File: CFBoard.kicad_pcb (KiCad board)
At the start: 2 copper layers, 80 x 60 mm, 21 parts, among them U1 STM32 Blue Pill, U2 Wemos D1 Mini, U3 GY-6500, U4 BMP180_5pin

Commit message: feat: wrap up version 1
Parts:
- moved R4 45.2 mm to (159.6, 113.2), turned to -90 degrees
- moved R3 27.4 mm to (111.1, 117.7)
- moved C5 25.2 mm to (137.9, 131.7)
- moved R5 18.5 mm to (148.4, 93.2), turned to 180 degrees
- moved C4 17.8 mm to (137.9, 97.2)
- moved U3 17.8 mm to (148.4, 108.7)
- moved REG1 17.8 mm to (170.4, 87.7)
- moved C1 17.8 mm to (154.1, 92.0)
- moved C3 17.8 mm to (158.1, 123.7)
- moved CONN1 17.8 mm to (142.6, 82.0)
- moved REF** 17.8 mm to (185.4, 81.0)
- moved REF** 17.8 mm to (110.9, 81.0)
- moved C2 17.8 mm to (184.9, 89.0)
- moved D2 17.8 mm to (158.1, 132.5)
- moved REF** 17.8 mm to (110.9, 135.5)
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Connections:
- C5 pad 1: Net-(U2-3.3V) -> Net-(D2-A)
- C5 pad 2: Net-(D2-A) -> Net-(U2-3.3V)
- R5 pad 1: Net-(U1-PB9) -> Net-(U3-INT)
- U3 pad 8: Net-(U1-PB9) -> Net-(U3-INT)
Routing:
- net Net-(D2-A): track 0.00 -> 196.8 mm
- net Net-(U2-Rx): track 0.00 -> 119.7 mm
- net Net-(U2-Tx): track 0.00 -> 105.8 mm
- net Net-(U2-3.3V): track 0.00 -> 85.8 mm, vias 0 -> 2
- net Net-(U1-PB8): track 0.00 -> 75.6 mm
- net Net-(U1-PB9): track 0.00 -> 70.1 mm
- net Net-(CONN1-Signal_2): track 0.00 -> 69.0 mm
- net Net-(CONN1-Signal_1): track 0.00 -> 64.9 mm
- net Net-(CONN1-Signal_3): track 0.00 -> 62.6 mm
- net Net-(CONN1-Signal_4): track 0.00 -> 61.5 mm
- net Net-(REG1-VOUT+): track 0.00 -> 46.4 mm
- net Net-(U2-D5): track 0.00 -> 37.9 mm
- net Net-(CONN1-VIN): track 0.00 -> 31.5 mm
- net Net-(U3-INT): track 0.00 -> 29.0 mm
- net Net-(CONN1-GND): track 0.00 -> 26.5 mm
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
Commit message: chore: fix trace
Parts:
- added D1: 1N5819, Diode_THT:D_DO-41_SOD81_P7.62mm_Horizontal, F.Cu at (159.5, 107.1)
- added SW1: Slide Switch, Button_Switch_THT:SW_Slide-03_Wuerth-WS-SLTV_10x2.5x6.4_P2.54mm, F.Cu at (111.0, 97.5)
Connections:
- C1 pad 1: Net-(CONN1-VIN) -> Net-(REG1-VIN+)
- C3 pad 1: Net-(U2-3.3V) -> Net-(D1-K)
- C4 pad 1: Net-(U2-3.3V) -> Net-(D1-A)
- C5 pad 2: Net-(U2-3.3V) -> Net-(D1-A)
- REG1 pad 1: Net-(CONN1-VIN) -> Net-(REG1-VIN+)
- U1 pad 38: Net-(U2-3.3V) -> Net-(D1-A)
- U2 pad 16: Net-(U2-3.3V) -> Net-(D1-K)
- U3 pad 1: Net-(U2-3.3V) -> Net-(D1-A)
- U4 pad 1: Net-(U2-3.3V) -> Net-(D1-A)
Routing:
- net Net-(U2-3.3V): track 85.8 -> 0.00 mm, vias 2 -> 0
- net Net-(D1-A): track 0.00 -> 84.0 mm, vias 0 -> 2
- net Net-(REG1-VIN+): track 0.00 -> 79.3 mm
- net Net-(D1-K): track 0.00 -> 26.0 mm
- net Net-(CONN1-VIN): track 31.5 -> 48.7 mm
- net Net-(U2-Tx): track 105.8 -> 109.2 mm
- net Net-(U2-Rx): track 119.7 -> 121.6 mm
- net Net-(D2-A): track 196.8 -> 198.5 mm
- net Net-(U1-PB9): track 70.1 -> 71.2 mm

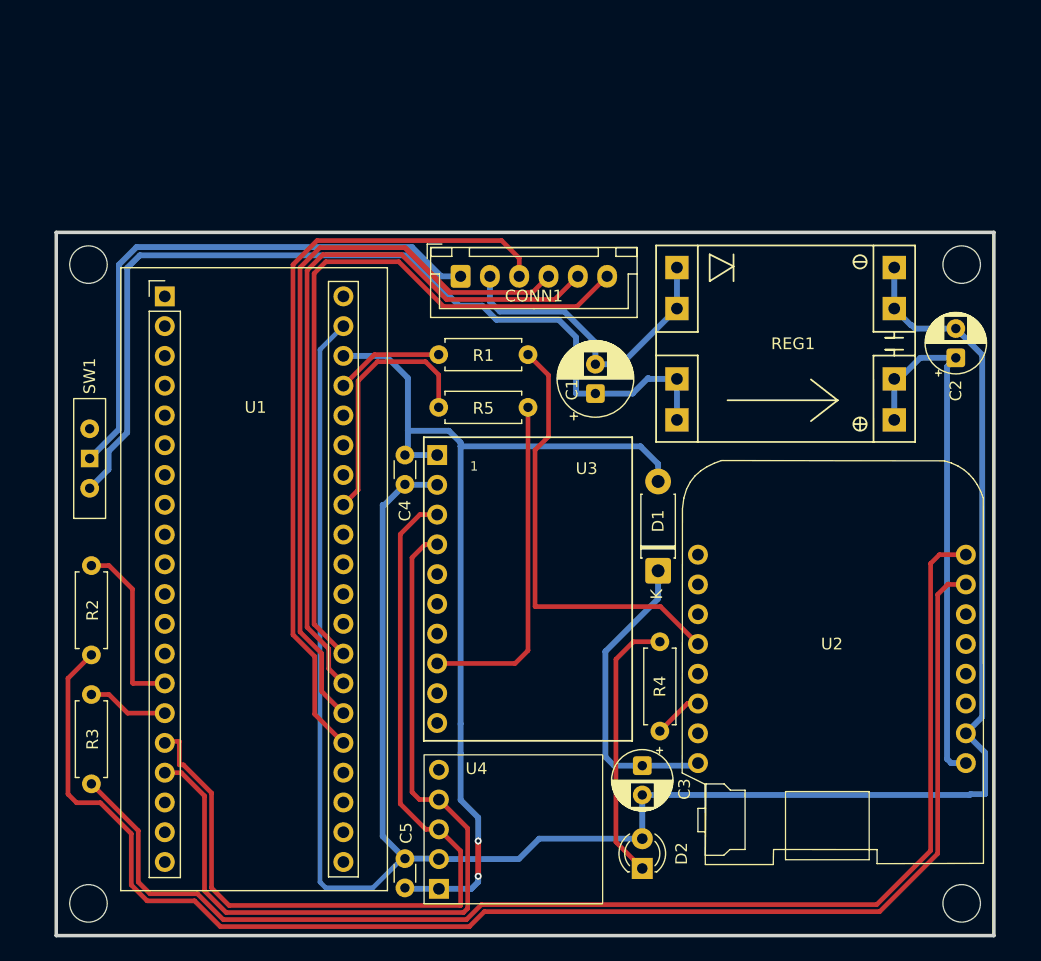
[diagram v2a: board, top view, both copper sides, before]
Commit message: feat: add silkscreen name and re-trace
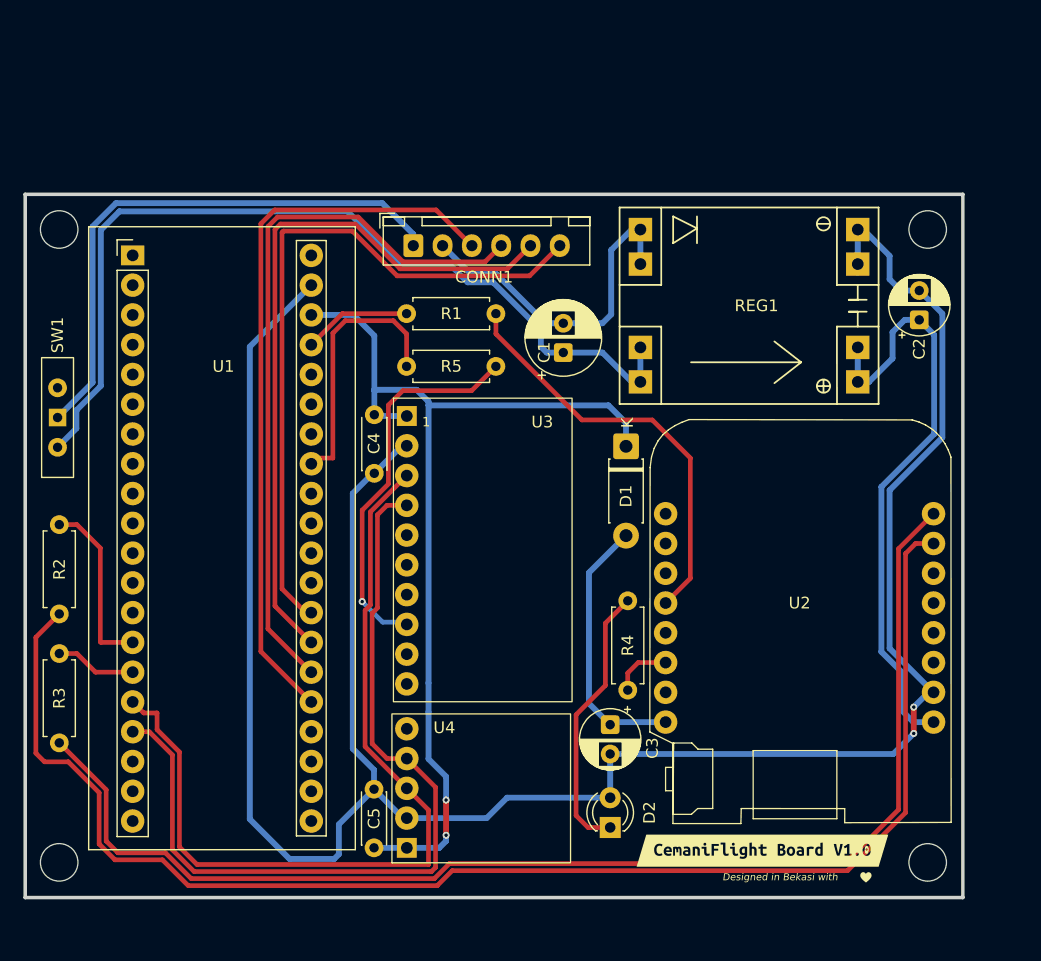
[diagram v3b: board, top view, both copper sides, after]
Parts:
- added kibuzzard-68789E7E: G***, kibuzzard-68789E7E, F.Cu at (168.4, 131.0)
- C4, C5: footprint Capacitor_THT:C_Disc_D3.0mm_W1.6mm_P2.50mm -> Capacitor_THT:C_Disc_D4.3mm_W1.9mm_P5.00mm
- CONN1: footprint Connector_JST:JST_XH_B6B-XH-A_1x06_P2.50mm_Vertical -> JST_XH_6Pin_Horizontal:JST_XH_6Pin_Horizontal
- moved D1 11.0 mm to (156.8, 96.5), turned to -90 degrees
- moved C5 6.48 mm to (135.3, 125.8)
- moved U3 5.10 mm to (144.5, 105.3)
- moved CONN1 4.81 mm to (138.6, 79.4)
- moved REF** 4.54 mm to (182.5, 132.0)
- moved REG1 4.50 mm to (167.3, 84.5)
- moved C2 4.50 mm to (181.8, 85.7)
- moved U2 4.45 mm to (171.6, 109.9)
- moved C1 4.44 mm to (151.4, 88.5)
- moved C3 4.44 mm to (155.4, 120.2)
- moved SW1 4.44 mm to (108.3, 94.0)
- moved U1 4.44 mm to (114.7, 80.2)
- moved D2 4.44 mm to (155.4, 129.0)
- moved R1 4.44 mm to (145.7, 85.2)
- moved R2 4.44 mm to (108.4, 103.2)
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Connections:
- C3 pad 1: Net-(D1-K) -> Net-(D1-A)
- C4 pad 1: Net-(D1-A) -> Net-(D1-K)
- C5 pad 2: Net-(D1-A) -> Net-(D1-K)
- U1 pad 38: Net-(D1-A) -> Net-(D1-K)
- U2 pad 16: Net-(D1-K) -> Net-(D1-A)
- U3 pad 1: Net-(D1-A) -> Net-(D1-K)
- U4 pad 1: Net-(D1-A) -> Net-(D1-K)
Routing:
- net Net-(D1-A): track 84.0 -> 23.3 mm, vias 2 -> 0
- net Net-(D1-K): track 26.0 -> 85.2 mm, vias 0 -> 2
- net Net-(CONN1-Signal_2): track 69.0 -> 61.9 mm
- net Net-(REG1-VOUT+): track 46.4 -> 51.9 mm
- net Net-(D2-A): track 198.5 -> 203.8 mm, vias 0 -> 2
- net Net-(U3-INT): track 29.0 -> 32.8 mm, vias 0 -> 1
- net Net-(REG1-VIN+): track 79.3 -> 76.6 mm
- net Net-(CONN1-Signal_1): track 64.9 -> 62.3 mm
- net Net-(CONN1-GND): track 27.0 -> 29.2 mm
- net Net-(U2-D5): track 37.9 -> 36.0 mm
- net Net-(CONN1-Signal_3): track 62.6 -> 60.9 mm
- net Net-(CONN1-Signal_4): track 61.5 -> 60.1 mm
- net Net-(U2-Tx): track 109.2 -> 107.9 mm
- net Net-(U1-PB8): track 75.9 -> 75.0 mm
- net Net-(CONN1-VIN): track 48.7 -> 47.8 mm
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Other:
- board text added: "Designed in Bekasi with"

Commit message: feat: generate gerbers
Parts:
- removed the REF** at (108.4, 132.0)
- removed the REF** at (182.5, 78.0)
- removed the REF** at (108.4, 78.0)
- removed the REF** at (182.5, 132.0)
- added REF**: MountingHole_3.2mm_M3_DIN965, MountingHole:MountingHole_3.2mm_M3_DIN965, F.Cu at (182.5, 132.0)
- added REF**: MountingHole_3.2mm_M3_DIN965, MountingHole:MountingHole_3.2mm_M3_DIN965, F.Cu at (108.5, 132.0)
- added REF**: MountingHole_3.2mm_M3_DIN965, MountingHole:MountingHole_3.2mm_M3_DIN965, F.Cu at (182.5, 78.0)
- added REF**: MountingHole_3.2mm_M3_DIN965, MountingHole:MountingHole_3.2mm_M3_DIN965, F.Cu at (108.5, 78.0)
- CONN1: footprint JST_XH_6Pin_Horizontal:JST_XH_6Pin_Horizontal -> Connector_JST:JST_XH_B6B-XH-A_1x06_P2.50mm_Vertical
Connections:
- net Net-(CONN1-GND) renamed GNDPWR
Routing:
- net Net-(D2-A): track 203.8 -> 200.9 mm
- net Net-(U1-PB8): track 75.0 -> 73.5 mm
- net GNDPWR: track 29.2 -> 28.4 mm
- net Net-(REG1-VIN+): track 76.6 -> 75.8 mm
- net Net-(U1-PB0): track 22.7 -> 22.0 mm
- net Net-(D1-K): track 85.2 -> 84.5 mm
- net Net-(D1-A): track 23.3 -> 22.7 mm
- net Net-(REG1-VOUT+): track 51.9 -> 51.3 mm

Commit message: feat: update design
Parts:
- removed the REF** at (182.5, 132.0)
- removed the REF** at (108.5, 132.0)
- removed the REF** at (182.5, 78.0)
- removed the REF** at (108.5, 78.0)
- added REF**: MountingHole_3.2mm_M3_DIN965, MountingHole:MountingHole_3.2mm_M3_DIN965, F.Cu at (108.2, 132.3)
- added REF**: MountingHole_3.2mm_M3_DIN965, MountingHole:MountingHole_3.2mm_M3_DIN965, F.Cu at (182.8, 77.7)
- added REF**: MountingHole_3.2mm_M3_DIN965, MountingHole:MountingHole_3.2mm_M3_DIN965, F.Cu at (108.2, 77.7)
- added REF**: MountingHole_3.2mm_M3_DIN965, MountingHole:MountingHole_3.2mm_M3_DIN965, F.Cu at (182.8, 132.3)
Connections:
- net Net-(D1-K) renamed DIODPWR
- net Net-(D2-A) renamed GNDREG
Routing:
- net GNDREG: track 200.9 -> 0.00 mm, vias 2 -> 0
- net DIODPWR: track 84.5 -> 5.45 mm, vias 2 -> 0
- net Net-(REG1-VOUT+): track 51.3 -> 47.3 mm
- net Net-(U3-INT): track 32.6 -> 29.7 mm, vias 1 -> 0
- net Net-(U1-PB8): track 73.5 -> 75.0 mm, vias 0 -> 1
- net Net-(CONN1-VIN): track 47.8 -> 46.4 mm
- net Net-(REG1-VIN+): track 75.8 -> 74.9 mm
- net Net-(D1-A): track 22.7 -> 23.5 mm
- net Net-(U1-PB9): track 72.0 -> 72.6 mm, vias 0 -> 1
- added copper zone on F.Cu, net DIODPWR
- added copper zone on B.Cu, net GNDREG

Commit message: feat: update jst connector footprint design
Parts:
- removed kibuzzard-68789E7E: G***, kibuzzard-68789E7E
- added kibuzzard-689068BD: G***, kibuzzard-689068BD, F.Cu at (171.1, 131.2)
- D1: footprint Diode_THT:D_DO-41_SOD81_P7.62mm_Horizontal -> Diode_THT:D_DO-41_SOD81_P10.16mm_Horizontal
- moved D2 1.43 mm to (155.6, 130.4)
- moved C2 0.85 mm to (182.1, 86.5)
- moved R1 0.82 mm to (145.7, 86.0)
- moved R5 0.32 mm to (145.7, 90.0)
- moved D1 0.24 mm to (156.9, 96.3)
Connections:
- net DIODPWR renamed Net-(D1-K)
- net GNDREG renamed Net-(D2-A)
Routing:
- net Net-(U1-PB0): track 22.0 -> 14.2 mm
- net Net-(U1-PB9): track 72.6 -> 70.0 mm
- net Net-(U2-D5): track 36.0 -> 33.9 mm
- net Net-(REG1-VIN+): track 74.9 -> 76.9 mm
- net Net-(CONN1-Signal_2): track 61.9 -> 63.8 mm
- net Net-(CONN1-Signal_4): track 59.7 -> 61.5 mm
- net Net-(CONN1-Signal_3): track 60.9 -> 62.7 mm
- net Net-(CONN1-VIN): track 46.4 -> 48.0 mm
- net Net-(D1-A): track 23.5 -> 22.0 mm
- net Net-(D2-K): track 23.5 -> 24.3 mm
- net Net-(CONN1-Signal_1): track 62.3 -> 63.0 mm
- net GNDPWR: track 28.0 -> 27.4 mm
- net Net-(U1-PB8): track 75.0 -> 74.4 mm

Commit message: feat: update design
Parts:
- REG1: value MP1584 -> MP1584_buck_module
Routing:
- net Net-(D1-K): track 5.45 -> 0.01 mm
- net Net-(U1-PB9): track 70.0 -> 70.2 mm, vias 1 -> 0
- net Net-(U1-PB8): track 74.4 -> 74.2 mm, vias 1 -> 0
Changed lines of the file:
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@@
 			)
 		)
-		(property "Value" "MP1584"
+		(property "Value" "MP1584_buck_module"
 			(at 0.271 1.93 0)
 			(layer "F.Fab")
@@
 		)
 		(fp_line
-			(start -11.049 1.778)
-			(end -7.493 1.778)
+			(start -11.049 2.032)
+			(end -7.493 2.032)
 			(stroke
 				(width 0.15)
@@
 		(fp_line
 			(start -7.493 -8.382)
-			(end -7.493 -1.778)
+			(end -7.493 -2.032)
 			(stroke
 				(width 0.15)
@@
 		)
 		(fp_line
-			(start -7.493 -1.778)
-			(end -11.049 -1.778)
+			(start -7.493 -2.032)
+			(end -11.049 -2.032)
 			(stroke
 				(width 0.15)
@@
 		)
 		(fp_line
-			(start -7.493 1.778)
+			(start -7.493 2.032)
 			(end -7.493 8.382)
 			(stroke
@@
 		)
 		(fp_line
-			(start 7.493 -1.778)
+			(start 7.493 -2.032)
 			(end 7.493 -8.382)
 			(stroke
@@
 		)
 		(fp_line
-			(start 7.493 1.778)
-			(end 11.049 1.778)
+			(start 7.493 2.032)
+			(end 11.049 2.032)
 			(stroke
 				(width 0.15)
@@
 		(fp_line
 			(start 7.5 8.4)
-			(end 7.492616 1.778)
+			(end 7.492899 2.032)
 			(stroke
 				(width 0.15)
@@
 		)
 		(fp_line
-			(start 9.271 -1.778)
+			(start 9.271 -2.032)
 			(end 9.271 -0.508)
 			(stroke
@@
 		(fp_line
 			(start 9.271 0.508)
-			(end 9.271 1.778)
+			(end 9.271 2.032)
 			(stroke
 				(width 0.15)
@@
 		)
 		(fp_line
-			(start 11.049 -1.778)
-			(end 7.493 -1.778)
+			(start 11.049 -2.032)
+			(end 7.493 -2.032)
 			(stroke
 				(width 0.15)
@@
 		)
 		(pad "1" thru_hole rect
-			(at -9.271 3.556)
+			(at -9.271 3.81)
 			(size 2 2)
 			(drill 1)
@@
 		)
 		(pad "2" thru_hole rect
-			(at -9.271 -3.556)
+			(at -9.271 -3.81)
 			(size 2 2)
 			(drill 1)
@@
 		)
 		(pad "3" thru_hole rect
-			(at 9.271 3.556)
+			(at 9.271 3.81)
 			(size 2 2)
 			(drill 1)
@@
 		)
 		(pad "4" thru_hole rect
-			(at 9.271 -3.556)
+			(at 9.275 -3.81)
 			(size 2 2)
 			(drill 1)
@@
 	)
 	(segment
-		(start 152.5 119.400058)
-		(end 152.5 128)
+		(start 155 111.59)
+		(end 155 116.900058)
 		(width 0.4)
 		(layer "F.Cu")
@@
 	)
 	(segment
-		(start 152.5 128)
-		(end 154.94 130.44)
+		(start 153.375 118.525058)
+		(end 153.375 128.215)
 		(width 0.4)
 		(layer "F.Cu")
@@
 	)
 	(segment
-		(start 156.91 109.68)
-		(end 155 111.59)
+		(start 155 116.900058)
+		(end 153.375 118.525058)
 		(width 0.4)
 		(layer "F.Cu")
@@
 	)
 	(segment
-		(start 155 116.900058)
-		(end 152.5 119.400058)
+		(start 156.91 109.68)
+		(end 155 111.59)
 		(width 0.4)
 		(layer "F.Cu")
@@
 	)
 	(segment
-		(start 155 111.59)
-		(end 155 116.900058)
+		(start 153.375 128.215)
+		(end 155.6 130.44)
 		(width 0.4)
 		(layer "F.Cu")
@@
 	)
 	(segment
-		(start 118.059 122.829)
-		(end 116.08 120.85)
-		(width 0.4)
-		(layer "F.Cu")
-		(net 14)
-	)
-	(segment
 		(start 116.08 120.85)
-		(end 114.67 120.85)
+		(end 118.059 122.829)
 		(width 0.4)
 		(layer "F.Cu")
@@
 	)
 	(segment
-		(start 135.875 120.955)
-		(end 138.06 123.14)
+		(start 114.67 120.85)
+		(end 116.08 120.85)
 		(width 0.4)
 		(layer "F.Cu")
@@
 	)
 	(segment
-		(start 138.056 101.5345)
-		(end 135.875 103.7155)
+		(start 119.911058 132.781)
+		(end 140.158942 132.781)
 		(width 0.4)
 		(layer "F.Cu")
@@
 	)
 	(segment
-		(start 118.059 130.928942)
-		(end 118.059 122.829)
+		(start 135.875 120.955)
+		(end 138.06 123.14)
 		(width 0.4)
 		(layer "F.Cu")
@@
 	)
 	(segment
-		(start 120 132.682)
-		(end 119.812058 132.682)
+		(start 118.059 122.829)
+		(end 118.059 130.928942)
 		(width 0.4)
 		(layer "F.Cu")
@@
 	)
 	(segment
-		(start 119.812058 132.682)
-		(end 118.059 130.928942)
+		(start 141.437029 126.517029)
+		(end 138.06 123.14)
 		(width 0.4)
 		(layer "F.Cu")
 		(net 14)
 	)
-	(via
-		(at 120 132.682)
-		(size 0.6)
-		(drill 0.3)
-		(layers "F.Cu" "B.Cu")
-		(net 14)
-	)
 	(segment
-		(start 138.06 123.14)
-		(end 141.25 126.33)
+		(start 138.056 101.5345)
+		(end 135.875 103.7155)
 		(width 0.4)
-		(layer "B.Cu")
+		(layer "F.Cu")
 		(net 14)
 	)
 	(segment
-		(start 141.25 131.75)
-		(end 140.318 132.682)
+		(start 141.437029 131.502913)
+		(end 141.437029 126.517029)
 		(width 0.4)
-		(layer "B.Cu")
+		(layer "F.Cu")
 		(net 14)
 	)
 	(segment
-		(start 141.25 126.33)
-		(end 141.25 131.75)
+		(start 118.059 130.928942)
+		(end 119.911058 132.781)
 		(width 0.4)
-		(layer "B.Cu")
+		(layer "F.Cu")
 		(net 14)
 	)
 	(segment
-		(start 140.318 132.682)
-		(end 120 132.682)
+		(start 140.158942 132.781)
+		(end 141.437029 131.502913)
 		(width 0.4)
-		(layer "B.Cu")
+		(layer "F.Cu")
 		(net 14)
 	)
@@
 	)
 	(segment
-		(start 116.75 120.670058)
-		(end 116.75 119.25)
+		(start 140.836029 128.456029)
+		(end 140.836029 131.253971)
 		(width 0.4)
 		(layer "F.Cu")
@@
 	)
 	(segment
-		(start 135.274 103.466558)
-		(end 135.274 122.894)
+		(start 118.66 120.36)
+		(end 116.61 118.31)
 		(width 0.4)
 		(layer "F.Cu")
@@
 	)
 	(segment
-		(start 120.001003 131.880994)
-		(end 119.860994 131.880994)
+		(start 120.16 132.18)
+		(end 119.7275 131.7475)
 		(width 0.4)
 		(layer "F.Cu")
@@
 	)
 	(segment
-		(start 136.545279 102.195279)
-		(end 135.274 103.466558)
+		(start 135.274 103.466558)
+		(end 135.274 122.894)
 		(width 0.4)
 		(layer "F.Cu")
@@
 	)
 	(segment
-		(start 118.66 130.68)
-		(end 118.66 122.580058)
+		(start 116.61 118.31)
+		(end 114.67 118.31)
 		(width 0.4)
 		(layer "F.Cu")
@@
 	)
 	(segment
-		(start 138.056 98.9945)
-		(end 136.545279 100.505221)
+		(start 136.545279 102.195279)
+		(end 135.274 103.466558)
 		(width 0.4)
 		(layer "F.Cu")
@@
 	)
 	(segment
-		(start 119.860994 131.880994)
-		(end 118.66 130.68)
+		(start 138.056 98.9945)
+		(end 136.545279 100.505221)
 		(width 0.4)
 		(layer "F.Cu")
@@
 	)
 	(segment
-		(start 118.66 122.580058)
-		(end 116.75 120.670058)
+		(start 139.91 132.18)
+		(end 120.16 132.18)
 		(width 0.4)
 		(layer "F.Cu")
@@
 	)
 	(segment
-		(start 115.61 119.25)
-		(end 114.67 118.31)
+		(start 119.860994 131.880994)
+		(end 118.66 130.68)
 		(width 0.4)
 		(layer "F.Cu")
@@
 	)
 	(segment
-		(start 135.274 122.894)
-		(end 138.06 125.68)
+		(start 140.836029 131.253971)
+		(end 139.91 132.18)
 		(width 0.4)
 		(layer "F.Cu")
@@
 	)
 	(segment
-		(start 116.75 119.25)
-		(end 115.61 119.25)
+		(start 118.66 130.68)
+		(end 118.66 120.36)
 		(width 0.4)
 		(layer "F.Cu")
 		(net 31)
 	)
-	(via
-		(at 120.001003 131.880994)
-		(size 0.6)
-		(drill 0.3)
-		(layers "F.Cu" "B.Cu")
-		(net 31)
-	)
 	(segment
-		(start 120.390364 132.081)
-		(end 120.190358 131.880994)
+		(start 135.274 122.894)
+		(end 138.06 125.68)
 		(width 0.4)
-		(layer "B.Cu")
+		(layer "F.Cu")
 		(net 31)
 	)
 	(segment
 		(start 138.06 125.68)
-		(end 139.750058 125.68)
-		(width 0.4)
-		(layer "B.Cu")
-		(net 31)
-	)
-	(segment
-		(start 140.649 126.578942)
-		(end 140.649 131.5)
-		(width 0.4)
-		(layer "B.Cu")
-		(net 31)
-	)
-	(segment
-		(start 139.750058 125.68)
-		(end 140.649 126.578942)
-		(width 0.4)
-		(layer "B.Cu")
-		(net 31)
-	)
-	(segment
-		(start 140.649 131.5)
-		(end 140.068 132.081)
-		(width 0.4)
-		(layer "B.Cu")
-		(net 31)
-	)
-	(segment
-		(start 120.190358 131.880994)
-		(end 120.001003 131.880994)
+		(end 140.836029 128.456029)
 		(width 0.4)
-		(layer "B.Cu")
-		(net 31)
-	)
-	(segment
-		(start 140.068 132.081)
-		(end 120.390364 132.081)
-		(width 0.4)
-		(layer "B.Cu")
+		(layer "F.Cu")
 		(net 31)
 	)
@@
 	)
 	(segment
-		(start 135.261 130.7545)
-		(end 138.0545 130.7545)
-		(width 1)
-		(layer "F.Cu")
-		(net 65)
-	)
-	(segment
-		(start 135.286 93.8045)
-		(end 137.946 93.8045)
+		(start 138.0545 130.7545)
+		(end 138.06 130.76)
 		(width 1)
 		(layer "F.Cu")
@@
 		(layer "F.Cu")
 		(hatch edge 0.5)
-		(connect_pads
+		(connect_pads yes
 			(clearance 0.5)
 		)
@@
 		(filled_areas_thickness no)
 		(fill yes
-			(thermal_gap 0.5)
+			(thermal_gap 0.25)
 			(thermal_bridge_width 1)
 		)
@@
 		(hatch edge 0.5)
 		(priority 1)
-		(connect_pads
+		(connect_pads yes
 			(clearance 0.5)
 		)
